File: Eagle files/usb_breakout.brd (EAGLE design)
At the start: 21.3 x 35.5 mm, 13 parts

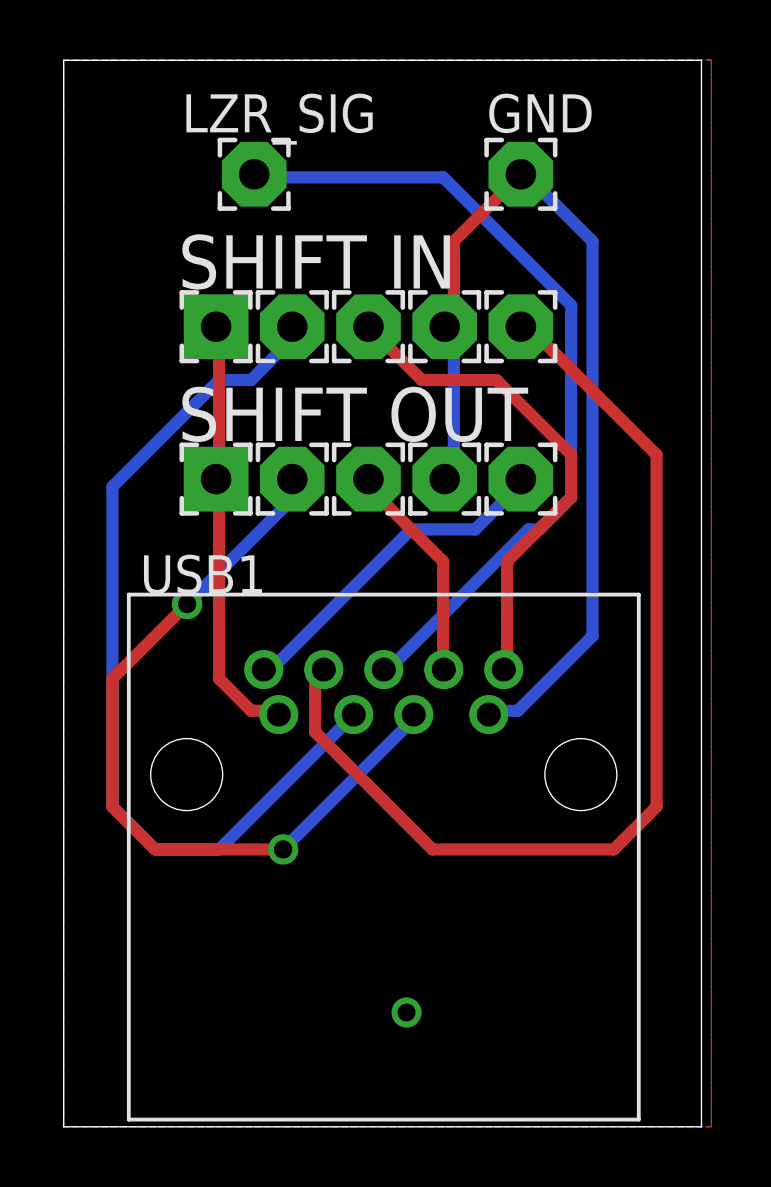
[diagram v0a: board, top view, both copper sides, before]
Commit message: Prep for oshpark
Changed naming of BarGraphDriver to be more accurate, added a new bar
graph driver for non-lv boards, fixed the usb breakout to match our
standards and removed the text doc.
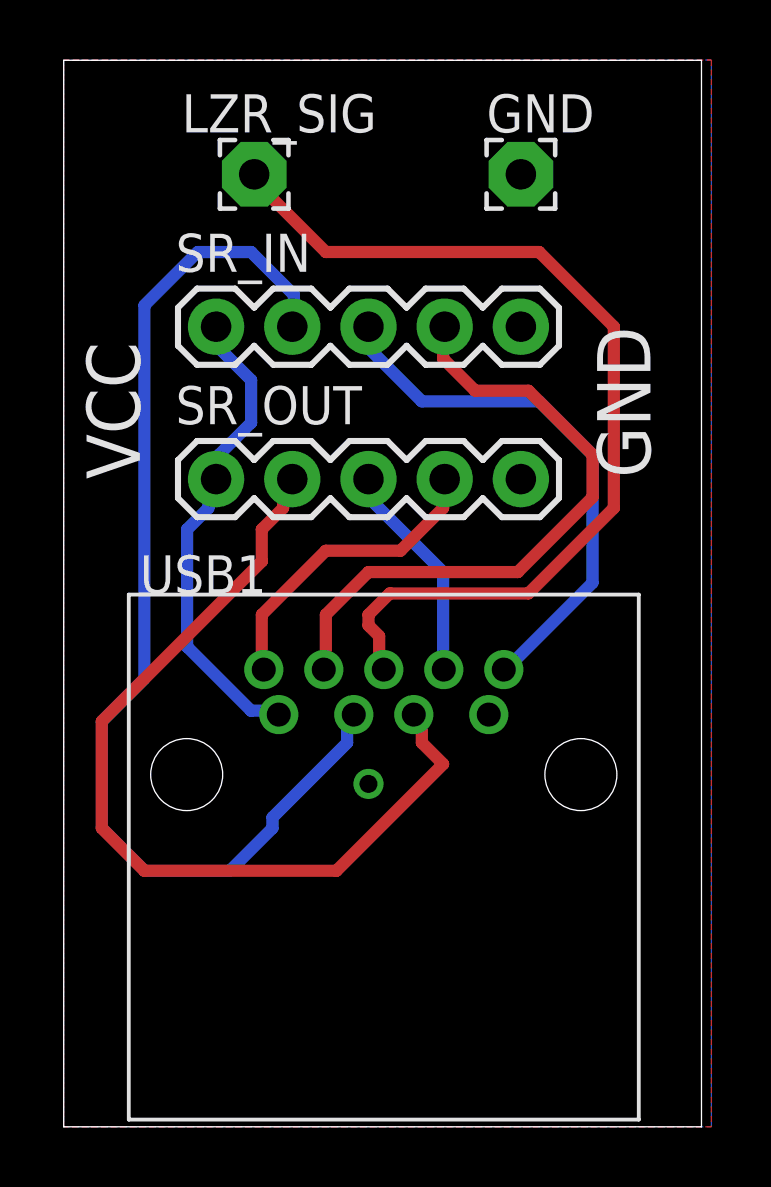
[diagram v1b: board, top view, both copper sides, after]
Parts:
- removed DATA_IN, DATA_OUT, GND_IN, GND_OUT, RCLK_IN, RCLK_OUT, SRCLK_IN, SRCLK_OUT: WIREPAD2,15/1,0, wirepad:2,15/1,0
- removed VCC_IN, VCC_OUT: WIREPAD2,15/1,0, smallWirepadSquare:2,15/1,0
- added SR_IN, SR_OUT: (no value), SparkFun-Connectors:1X05
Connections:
- net DATA_IN: now also SR_IN.4; no longer DATA_IN.1
- net DATA_OUT: now also SR_OUT.4; no longer DATA_OUT.1
- net GND: now also SR_IN.5, SR_OUT.5; no longer GND_IN.1, GND_OUT.1
- net RCLK_IN: now also SR_IN.2; no longer RCLK_IN.1
- net RCLK_OUT: now also SR_OUT.2; no longer RCLK_OUT.1
- net SRCLK_IN: now also SR_IN.3; no longer SRCLK_IN.1
- net SRCLK_OUT: now also SR_OUT.3; no longer SRCLK_OUT.1
- net VCC: now also SR_IN.1, SR_OUT.1; no longer VCC_IN.1, VCC_OUT.1
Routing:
- net GND: track 32.9 -> 0.00 mm
- net DATA_IN: track 33.8 -> 21.2 mm
- net RCLK_IN: track 29.8 -> 37.2 mm
- net LZR_SIG: track 27.4 -> 32.1 mm
- net RCLK_OUT: track 26.0 -> 29.8 mm, vias 2 -> 0
- net VCC: track 14.4 -> 16.1 mm
- net SRCLK_IN: track 16.6 -> 18.1 mm
- net DATA_OUT: track 11.3 -> 10.3 mm
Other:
- board text added: "GND"
- board text added: "VCC"
- board text removed: "SHIFT IN"
- board text removed: "SHIFT OUT"

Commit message: aaaaaaaaaaaaaaaaaaaaaaaaaaaaaaaaaaaa
Cleaned up schematics, replaced wire solder points with header pin
mounts for standardization, recreated a broken file and dealt with the
confusion and insanity that followed.
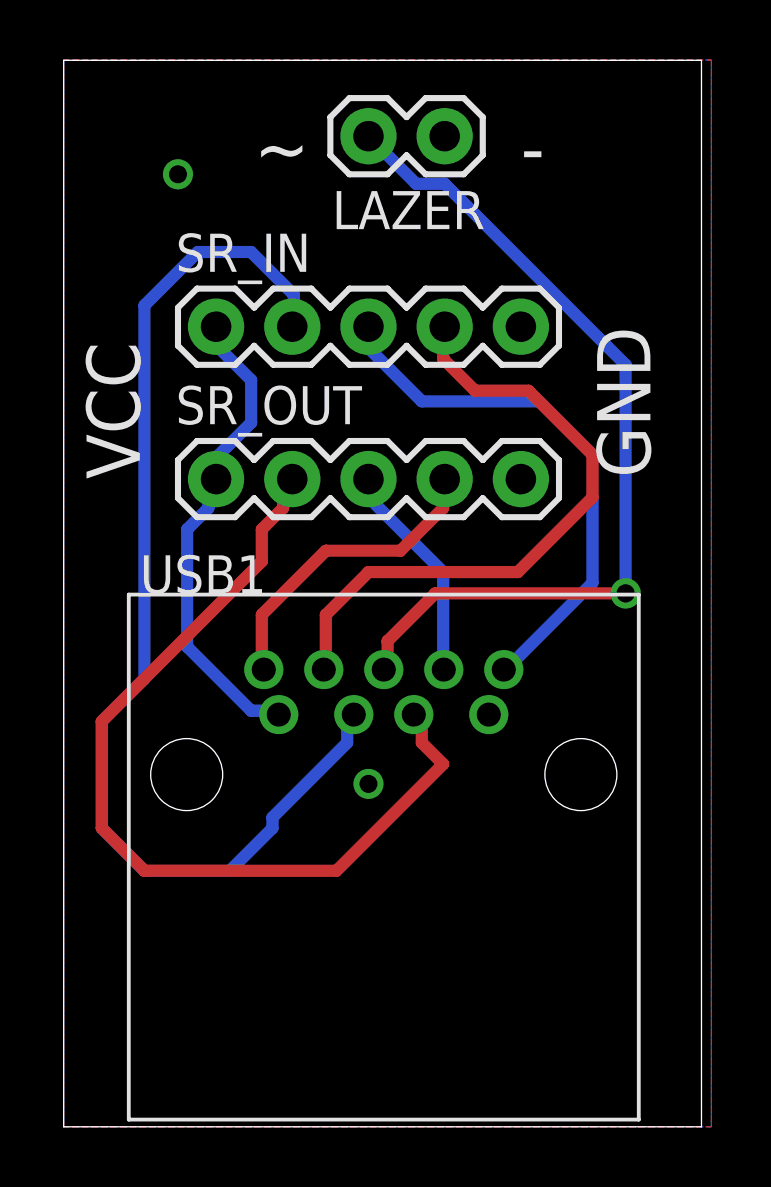
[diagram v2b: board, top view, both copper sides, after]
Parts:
- removed GND, LZR_SIG: WIREPAD2,15/1,0, wirepad:2,15/1,0
- added LAZER: (no value), SparkFun-Connectors:1X02
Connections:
- net GND: now also LAZER.1; no longer GND.1
- net LZR_SIG: now also LAZER.2; no longer LZR_SIG.1
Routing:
- net LZR_SIG: track 32.1 -> 29.0 mm, vias 0 -> 1
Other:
- board text added: "-"
- board text added: "~"
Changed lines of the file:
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@@
 <text x="1.27" y="21.59" size="1.778" layer="25" rot="R90">VCC</text>
 <text x="16.51" y="26.67" size="1.778" layer="25" rot="R270">GND</text>
+<text x="13.97" y="31.75" size="1.778" layer="25">-</text>
+<text x="5.08" y="31.75" size="1.778" layer="25">~</text>
 </plain>
 <attributes>
@@
 <elements>
 <element name="USB1" library="my_try" package="48405-0003MYVERSION" value="48405-0003" x="16.51" y="16.51"/>
-<element name="LZR_SIG" library="wirepad" package="2,15/1,0" value="WIREPAD2,15/1,0" x="5.08" y="31.75" smashed="yes" rot="R90">
-<attribute name="NAME" x="2.667" y="33.147" size="1.27" layer="25" ratio="10"/>
-<attribute name="VALUE" x="4.08" y="30.48" size="0.0254" layer="27" rot="R90"/>
-</element>
-<element name="GND" library="wirepad" package="2,15/1,0" value="WIREPAD2,15/1,0" x="13.97" y="31.75" smashed="yes" rot="R90">
-<attribute name="NAME" x="12.827" y="33.147" size="1.27" layer="25" ratio="10"/>
-<attribute name="VALUE" x="12.97" y="31.75" size="0.0254" layer="27" rot="R90"/>
-</element>
 <element name="SR_IN" library="SparkFun-Connectors" package="1X05" value="" x="3.81" y="26.67"/>
 <element name="SR_OUT" library="SparkFun-Connectors" package="1X05" value="" x="3.81" y="21.59"/>
+<element name="LAZER" library="SparkFun-Connectors" package="1X02" value="" x="11.43" y="33.02" rot="R180"/>
 </elements>
 <signals>
@@
 <signal name="GND">
 <contactref element="USB1" pad="GND"/>
-<contactref element="GND" pad="1"/>
 <polygon width="0.4064" layer="16">
 <vertex x="20.32" y="35.56"/>
@@
 <contactref element="SR_OUT" pad="5"/>
 <via x="8.89" y="11.43" extent="1-16" drill="0.6"/>
+<contactref element="LAZER" pad="1"/>
+<via x="2.54" y="31.75" extent="1-16" drill="0.6" shape="square"/>
 </signal>
 <signal name="RCLK_OUT">
@@
 <signal name="LZR_SIG">
 <contactref element="USB1" pad="GND_DRAIN"/>
-<contactref element="LZR_SIG" pad="1"/>
-<wire x1="9.2456" y1="16.3576" x2="9.2456" y2="15.2908" width="0.4064" layer="1"/>
-<wire x1="8.89" y1="16.7132" x2="9.2456" y2="16.3576" width="0.4064" layer="1"/>
-<wire x1="8.89" y1="17.0688" x2="8.89" y2="16.7132" width="0.4064" layer="1"/>
-<wire x1="9.6012" y1="17.78" x2="8.89" y2="17.0688" width="0.4064" layer="1"/>
-<wire x1="14.224" y1="17.78" x2="9.6012" y2="17.78" width="0.4064" layer="1"/>
-<wire x1="17.0688" y1="20.6248" x2="14.224" y2="17.78" width="0.4064" layer="1"/>
-<wire x1="17.0688" y1="26.67" x2="17.0688" y2="20.6248" width="0.4064" layer="1"/>
-<wire x1="14.5796" y1="29.1592" x2="17.0688" y2="26.67" width="0.4064" layer="1"/>
-<wire x1="7.4676" y1="29.1592" x2="14.5796" y2="29.1592" width="0.4064" layer="1"/>
-<wire x1="4.9784" y1="31.6484" x2="7.4676" y2="29.1592" width="0.4064" layer="1"/>
-<wire x1="9.2456" y1="15.2908" x2="9.4" y2="15.24" width="0.4064" layer="1"/>
-<wire x1="4.9784" y1="31.6484" x2="5.08" y2="31.75" width="0.4064" layer="1"/>
+<contactref element="LAZER" pad="2"/>
+<wire x1="9.525" y1="16.1925" x2="9.525" y2="15.24" width="0.4064" layer="1"/>
+<wire x1="11.1125" y1="17.78" x2="9.525" y2="16.1925" width="0.4064" layer="1"/>
+<wire x1="17.4625" y1="17.78" x2="11.1125" y2="17.78" width="0.4064" layer="1"/>
+<wire x1="17.4625" y1="25.4" x2="17.4625" y2="17.78" width="0.4064" layer="16"/>
+<wire x1="11.43" y1="31.4325" x2="17.4625" y2="25.4" width="0.4064" layer="16"/>
+<wire x1="10.4775" y1="31.4325" x2="11.43" y2="31.4325" width="0.4064" layer="16"/>
+<wire x1="8.89" y1="33.02" x2="10.4775" y2="31.4325" width="0.4064" layer="16"/>
+<wire x1="9.525" y1="15.24" x2="9.4" y2="15.24" width="0.4064" layer="1"/>
+<via x="17.4625" y="17.78" extent="1-16" drill="0.6096"/>
 </signal>
 <signal name="RCLK_IN">
